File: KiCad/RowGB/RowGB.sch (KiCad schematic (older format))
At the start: 44 parts, among them P1 CONN_N, P2 CONN_W, P3 CONN_E, P4 CONN_S, P5 CONN_1, P6 CONN_1, P7 CONN_1, P8 CONN_1, U1 RGB_WS2811, U10 RGB_WS2811, U11 RGB_WS2811, U12 RGB_WS2811, U13 RGB_WS2811, U14 RGB_WS2811, U15 RGB_WS2811, U16 RGB_WS2811, U2 RGB_WS2811, U3 RGB_WS2811, U4 RGB_WS2811, U5 RGB_WS2811, U6 RGB_WS2811, U7 RGB_WS2811, U8 RGB_WS2811, U9 RGB_WS2811

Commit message: RowGB looks complete. Gerbers pending.
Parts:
- added C17: 47uF,10V, CP_5x11mm, symbol C_POL_1
- added PCB1: CONN_1, PCB, symbol CONN_1
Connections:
- net 5V: now also C17.1 (+)
- net GND: now also C17.2 (-)
- no-connect marks 20 -> 21
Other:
- note added: "PCB"

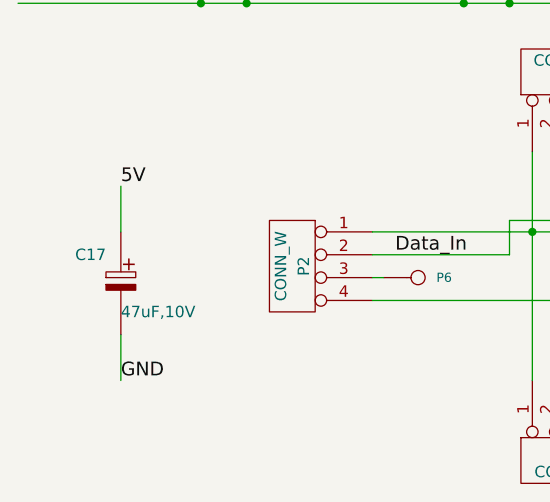
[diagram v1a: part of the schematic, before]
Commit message: RowGB complete. Gerbers ready for prototype boards. BoM ready.
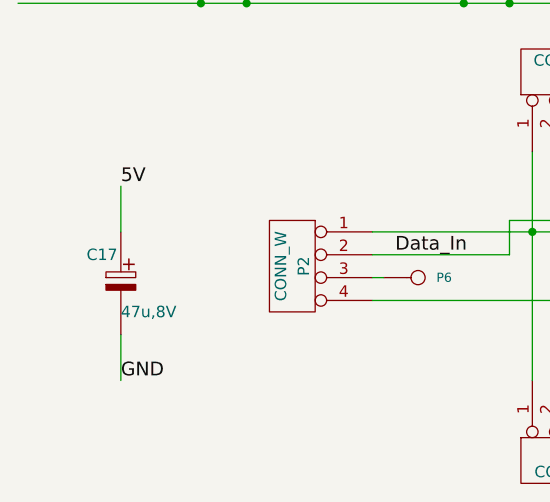
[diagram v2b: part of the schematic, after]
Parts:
- removed P3: CONN_E, CONN_E, symbol CONN4_S
- added P3: CONN_E, symbol CONN_E
- C17: value 47uF,10V -> 47u,8V; footprint CP_5x11mm -> c_2917; Field10 P833-ND -> PCE3606CT-ND; Field11 http://www.digikey.com/product-detail/en/ECE-A1CKA101/P833-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 -> http://www.digikey.com/product-detail/en/EEF-CD0K470R/PCE36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; Field4 CAP ALUM 100UF 16V 20% RADIAL -> CAP ALUM 47UF 8V 20% SMD; Field5 100u,16V -> 47u,8V; Field6 Radial, Can, 6.3mm dia -> 2917 (7343 Metric); Field8 ECE-A1CKA101 -> EEF-CD0K470R
- P2: footprint CONN_W -> (none); Field10 609-3317-ND -> SAM1031-50-ND; Field11 http://www.digikey.com/product-detail/en/68016-116HLF/609-3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 -> http://www.digikey.com/scripts/DkSearch/dksus.dll?WT.z_head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; Field4 CONN HEADER 16POS .100 R/A 30AU -> CONN HEADER 50POS .100\" SGL GOLD; Field6 0.1\" right angle -> 0.1\"; Field7 FCI -> Samtec Inc; Field8 68016-116HLF -> TSW-150-07-L-S
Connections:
- net 5V: now also P3.1 (P1)
- net Data_Out: now also P3.2 (P2)
- net GND: now also P3.4 (P4)
- net at P7.1: now also P3.3 (P3)
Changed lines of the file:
@@
-EESchema Schematic File Version 2  date Sunday 06 January 2013 05:57:23 PM IST
+EESchema Schematic File Version 2  date 1/7/2013 2:11:28 PM
 LIBS:RowGB_sym
 LIBS:RowGB-cache
@@
 Sheet 1 1
 Title ""
-Date "6 jan 2013"
+Date "7 jan 2013"
 Rev ""
 Comp ""
@@
 Comment4 ""
 $EndDescr
+$Comp
+L CONN_E P3
+U 1 1 50EA8A1D
+P 4600 6750
+F 0 "P3" V 4550 6750 50  0000 C CNN
+F 1 "CONN_E" V 4650 6750 50  0000 C CNN
+F 4 "CONN HEADER 50POS .100\" SGL GOLD" H 4600 6850 60  0001 L CNN "Field4"
+F 5 "Header, Unshrouded, Male pin," H 4600 6950 60  0001 L CNN "Field5"
+F 6 "0.1\"" H 4600 7050 60  0001 L CNN "Field6"
+F 7 "Samtec Inc" H 4600 7150 60  0001 L CNN "Field7"
+F 8 "TSW-150-07-L-S" H 4600 7250 60  0001 L CNN "Field8"
+F 9 "Digikey" H 4600 7350 60  0001 L CNN "Field9"
+F 10 "SAM1031-50-ND" H 4600 7450 60  0001 L CNN "Field10"
+F 11 "http://www.digikey.com/scripts/DkSearch/dksus.dll?WT.z_header=search_go&lang=en&keywords=SAM1031-50-ND&x=15&y=16&cur=USD" H 4600 7550 60  0001 L CNN "Field11"
+	1    4600 6750
+	1    0    0    -1
+$EndComp
+$Comp
+L CONN_W P2
+U 1 1 50EA89E6
+P 2200 6750
+F 0 "P2" V 2150 6750 50  0000 C CNN
+F 1 "CONN_W" V 2250 6750 50  0000 C CNN
+F 4 "CONN HEADER 50POS .100\" SGL GOLD" H 2200 6850 60  0001 L CNN "Field4"
+F 5 "Header, Unshrouded, Male pin," H 2200 6950 60  0001 L CNN "Field5"
+F 6 "0.1\"" H 2200 7050 60  0001 L CNN "Field6"
+F 7 "Samtec Inc" H 2200 7150 60  0001 L CNN "Field7"
+F 8 "TSW-150-07-L-S" H 2200 7250 60  0001 L CNN "Field8"
+F 9 "Digikey" H 2200 7350 60  0001 L CNN "Field9"
+F 10 "SAM1031-50-ND" H 2200 7450 60  0001 L CNN "Field10"
+F 11 "http://www.digikey.com/scripts/DkSearch/dksus.dll?WT.z_header=search_go&lang=en&keywords=SAM1031-50-ND&x=15&y=16&cur=USD" H 2200 7550 60  0001 L CNN "Field11"
+	1    2200 6750
+	-1   0    0    -1
+$EndComp
+$Comp
+L C_POL_1 C17
+U 1 1 50EA6BA3
+P 1450 6800
+F 0 "C17" H 1300 6900 50  0000 L CNN
+F 1 "47u,8V" H 1450 6650 50  0000 L CNN
+F 2 "c_2917" H 1450 6750 50  0001 C CNN
+F 4 "CAP ALUM 47UF 8V 20% SMD" H 1450 7000 60  0001 L CNN "Field4"
+F 5 "47u,8V" H 1450 7100 60  0001 L CNN "Field5"
+F 6 "2917 (7343 Metric)" H 1450 7200 60  0001 L CNN "Field6"
+F 7 "Panasonic Electronic Components" H 1450 7300 60  0001 L CNN "Field7"
+F 8 "EEF-CD0K470R" H 1450 7400 60  0001 L CNN "Field8"
+F 9 "Digikey" H 1450 7500 60  0001 L CNN "Field9"
+F 10 "PCE3606CT-ND" H 1450 7600 60  0001 L CNN "Field10"
+F 11 "http://www.digikey.com/product-detail/en/EEF-CD0K470R/PCE3606CT-ND/614442" H 1450 7700 60  0001 L CNN "Field11"
+	1    1450 6800
+	1    0    0    -1
+$EndComp
 Text Notes 6600 7050 0    60   ~ 0
 PCB
@@
 Wire Wire Line
 	1450 6600 1450 6400
-$Comp
-L C_POL_1 C17
-U 1 1 50E95E82
-P 1450 6800
-F 0 "C17" H 1250 6900 50  0000 L CNN
-F 1 "47uF,10V" H 1450 6650 50  0000 L CNN
-F 2 "CP_5x11mm" H 1450 6800 60  0001 C CNN
-F 4 "CAP ALUM 100UF 16V 20% RADIAL" H 1450 7000 60  0001 L CNN "Field4"
-F 5 "100u,16V" H 1450 7100 60  0001 L CNN "Field5"
-F 6 "Radial, Can, 6.3mm dia" H 1450 7200 60  0001 L CNN "Field6"
-F 7 "Panasonic Electronic Components" H 1450 7300 60  0001 L CNN "Field7"
-F 8 "ECE-A1CKA101" H 1450 7400 60  0001 L CNN "Field8"
-F 9 "Digikey" H 1450 7500 60  0001 L CNN "Field9"
-F 10 "P833-ND" H 1450 7600 60  0001 L CNN "Field10"
-F 11 "http://www.digikey.com/product-detail/en/ECE-A1CKA101/P833-ND/44757?cur=USD" H 1450 7700 60  0001 L CNN "Field11"
-	1    1450 6800
-	1    0    0    -1
-$EndComp
 Text Notes 5400 7050 0    60   ~ 0
 Mounting Screws
@@
 	1    3450 6450
 	0    1    1    0
-$EndComp
-$Comp
-L CONN4_S P3
-U 1 1 50E7F7C5
-P 4600 6750
-F 0 "P3" V 4550 6750 50  0000 C CNN
-F 1 "CONN_E" V 4650 6750 50  0000 C CNN
-F 2 "CONN_E" V 4750 6750 50  0001 C CNN
-F 4 "Conn Socket Strip SKT 5 POS 2.54mm Solder RA Thru-Hole" H 4600 6850 60  0001 L CNN "Field4"
-F 5 "Header, Female" H 4600 6950 60  0001 L CNN "Field5"
-F 6 "0.1\" right angle" H 4600 7050 60  0001 L CNN "Field6"
-F 7 "Samtec" H 4600 7150 60  0001 L CNN "Field7"
-F 8 "BCS-104-L-S-HE" H 4600 7250 60  0001 L CNN "Field8"
-F 9 "Arrow" H 4600 7350 60  0001 L CNN "Field9"
-F 10 "BCS-104-L-S-HE" H 4600 7450 60  0001 L CNN "Field10"
-F 11 "http://components.arrow.com/part/detail/2769370S3578027N1004" H 4600 7550 60  0001 L CNN "Field11"
-	1    4600 6750
-	1    0    0    -1
 $EndComp
 $Comp
@@
 5V
 $Comp
-L CONN_W P2
-U 1 1 50E7EA0C
-P 2200 6750
-F 0 "P2" V 2150 6750 50  0000 C CNN
-F 1 "CONN_W" V 2250 6750 50  0000 C CNN
-F 2 "CONN_W" V 2350 6750 50  0001 C CNN
-F 4 "CONN HEADER 16POS .100 R/A 30AU" H 2200 6850 60  0001 L CNN "Field4"
-F 5 "Header, Unshrouded, Male pin," H 2200 6950 60  0001 L CNN "Field5"
-F 6 "0.1\" right angle" H 2200 7050 60  0001 L CNN "Field6"
-F 7 "FCI" H 2200 7150 60  0001 L CNN "Field7"
-F 8 "68016-116HLF" H 2200 7250 60  0001 L CNN "Field8"
-F 9 "Digikey" H 2200 7350 60  0001 L CNN "Field9"
-F 10 "609-3317-ND" H 2200 7450 60  0001 L CNN "Field10"
-F 11 "http://www.digikey.com/product-detail/en/68016-116HLF/609-3317-ND/1878554" H 2200 7550 60  0001 L CNN "Field11"
-	1    2200 6750
-	-1   0    0    -1
-$EndComp
-$Comp
 L C2 C16

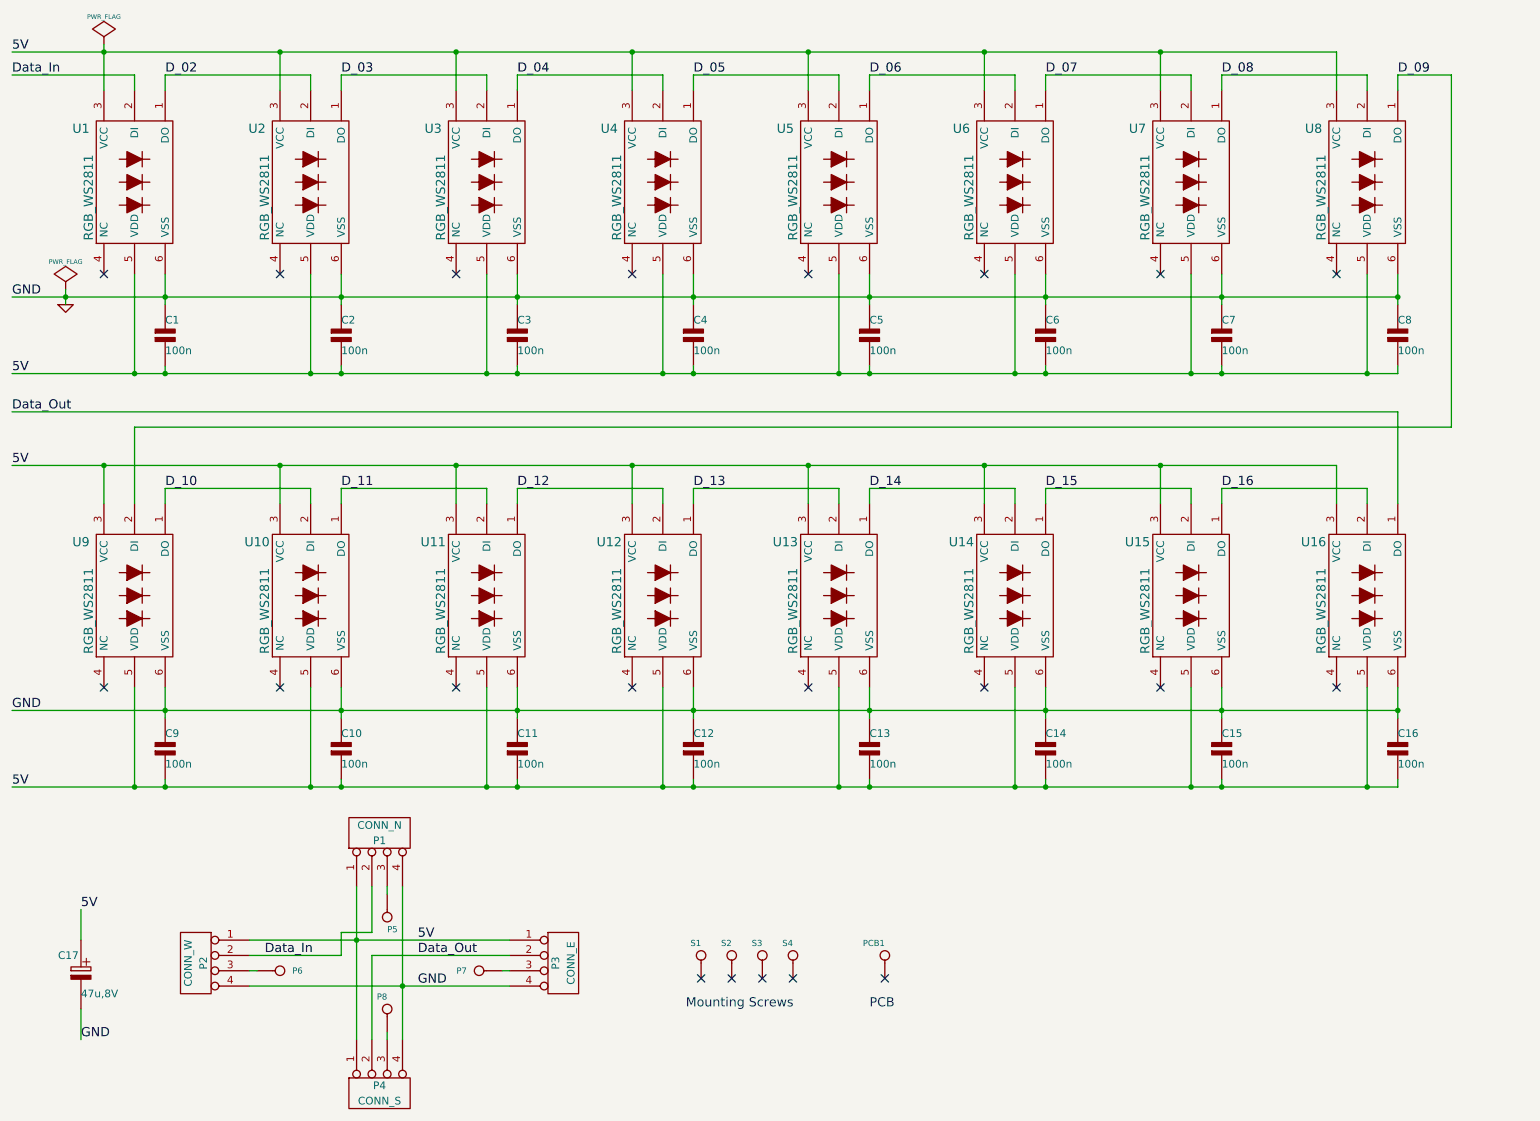
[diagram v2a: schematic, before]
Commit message: RowGB added ATTiny slave controller and Stack-L Stack-R (C3SB) connectors.
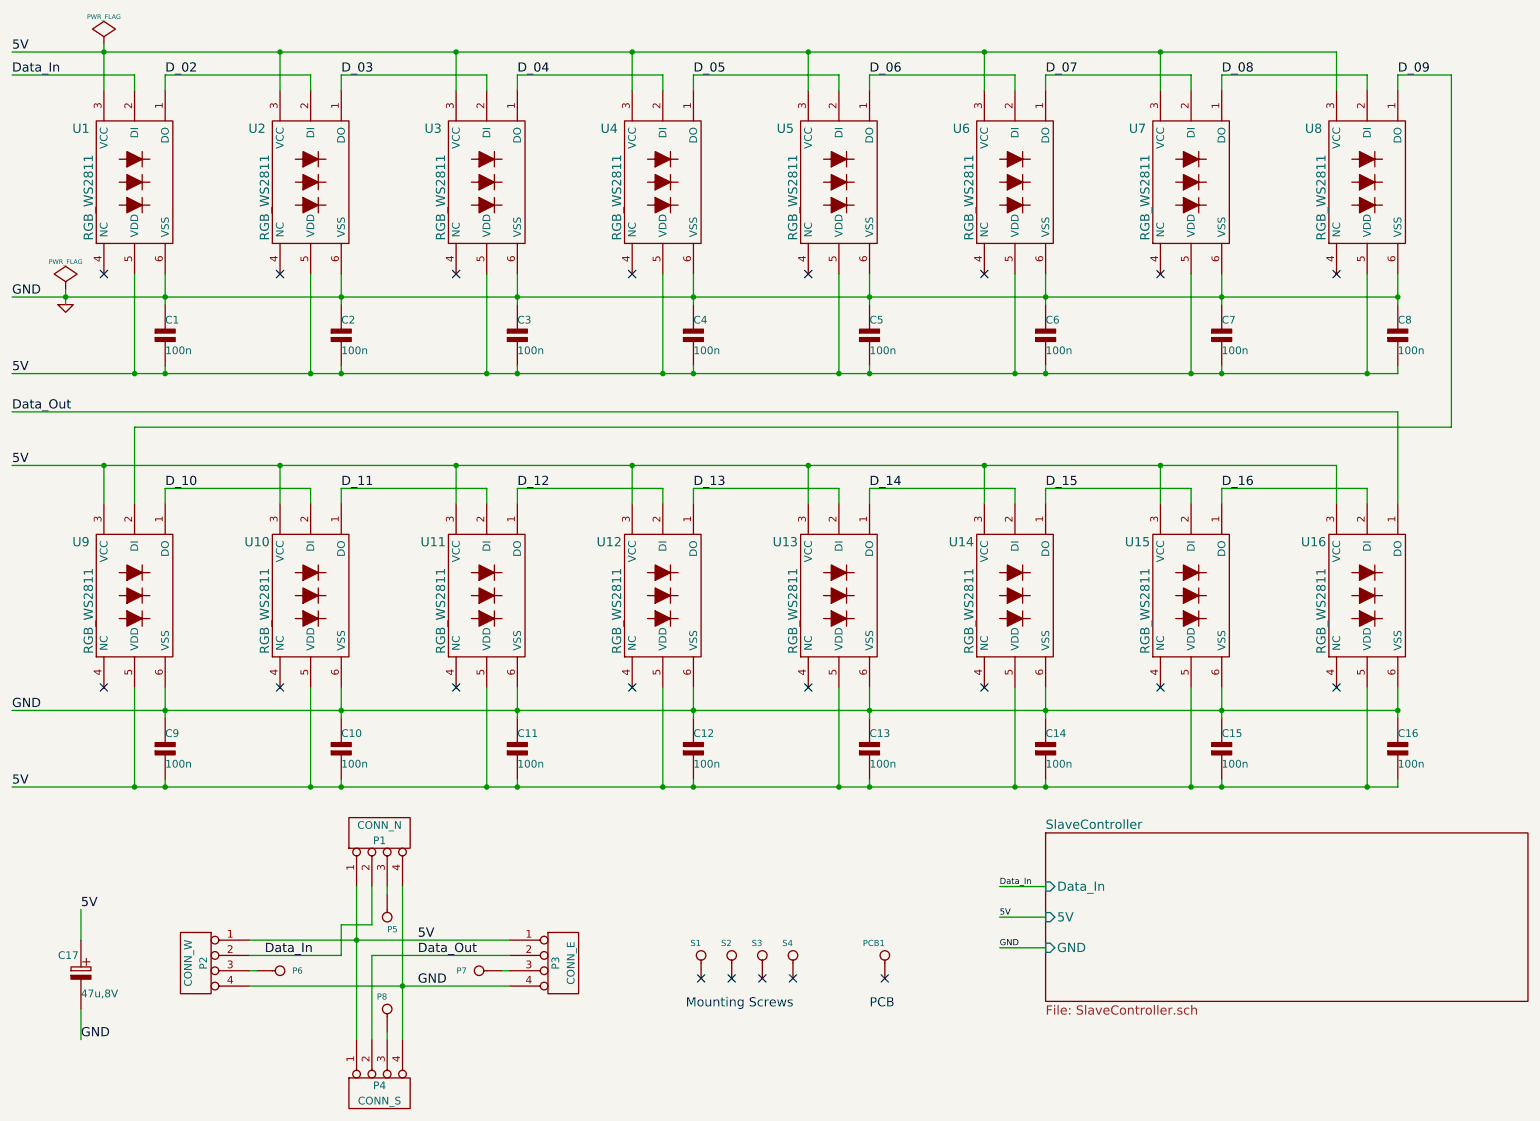
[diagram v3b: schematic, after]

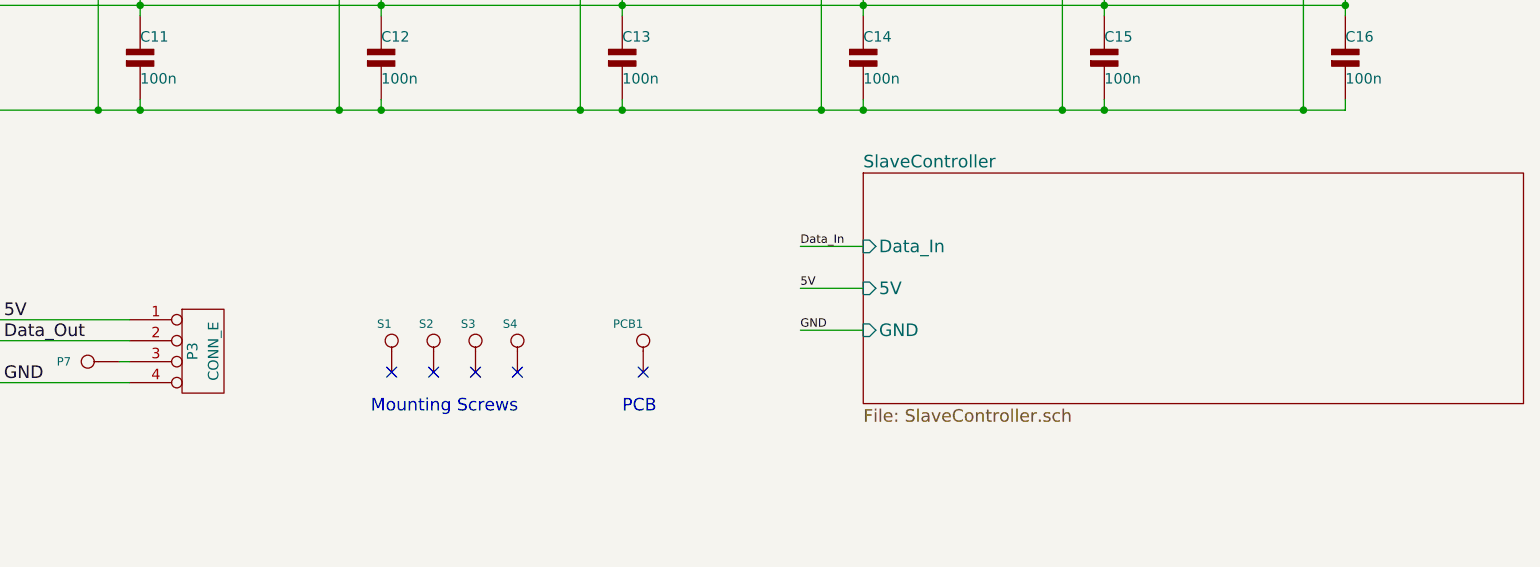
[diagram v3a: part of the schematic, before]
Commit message: RowGB - started work on larger matrix.
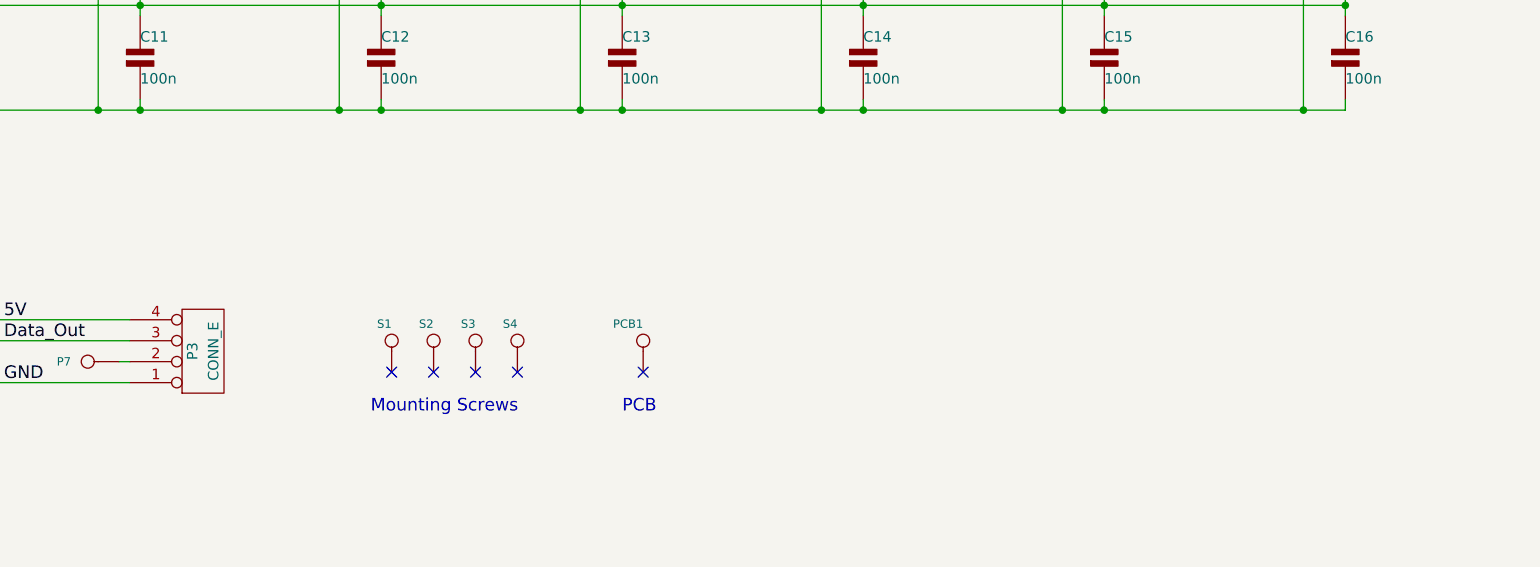
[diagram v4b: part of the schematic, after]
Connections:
- net 5V: now also P3.4 (P4); no longer P3.1 (P1)
- net Data_Out: now also P3.3 (P3); no longer P3.2 (P2)
- net GND: now also P3.1 (P1); no longer P3.4 (P4)
- net at P7.1: now also P3.2 (P2); no longer P3.3 (P3)
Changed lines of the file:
@@
-EESchema Schematic File Version 2  date Wednesday 09 January 2013 07:47:09 PM IST
+EESchema Schematic File Version 2  date 2/9/2013 2:40:07 PM
 LIBS:RowGB_sym
 LIBS:RowGB-cache
@@
 $Descr A4 11700 8267
 encoding utf-8
-Sheet 1 2
+Sheet 1 1
 Title ""
-Date "9 jan 2013"
+Date "9 feb 2013"
 Rev ""
 Comp ""
@@
 Comment4 ""
 $EndDescr
-Text Label 7450 6250 0    40   ~ 0
-Data_In
-Wire Wire Line
-	7750 6250 7450 6250
-Wire Wire Line
-	7750 6450 7450 6450
 Wire Wire Line
 	1450 6600 1450 6400
@@
 Wire Wire Line
 	1450 7050 1450 7250
-Wire Wire Line
-	7450 6650 7750 6650
-Text Label 7450 6650 0    40   ~ 0
-GND
-Text Label 7450 6450 0    40   ~ 0
-5V
-$Sheet
-S 7750 5900 3150 1100
-U 50ED424F
-F0 "SlaveController" 60
-F1 "SlaveController.sch" 60
-F2 "GND" I L 7750 6650 60
-F3 "5V" I L 7750 6450 60
-F4 "Data_In" I L 7750 6250 60
-$EndSheet
 $Comp
 L CONN_E P3
@@
 F 11 "http://www.digikey.com/scripts/DkSearch/dksus.dll?WT.z_header=search_go&lang=en&keywords=SAM1031-50-ND&x=15&y=16&cur=USD" H 4600 7550 60  0001 L CNN "Field11"
 	1    4600 6750
-	1    0    0    -1
+	1    0    0    1
 $EndComp
 $Comp
